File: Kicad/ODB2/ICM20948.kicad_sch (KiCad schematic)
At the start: 2 parts, among them U6 ICM-20948

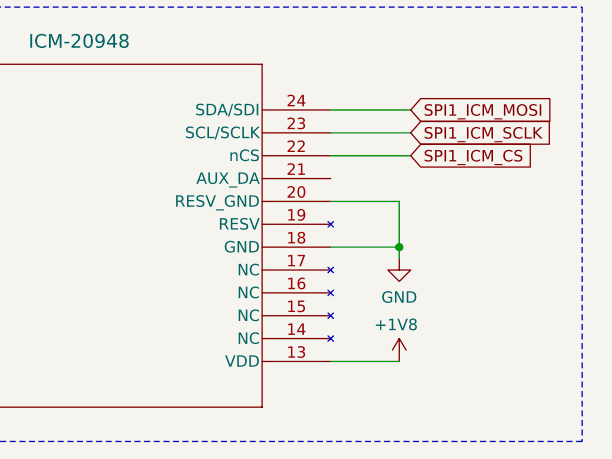
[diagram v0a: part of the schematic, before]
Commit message: add C decoupling
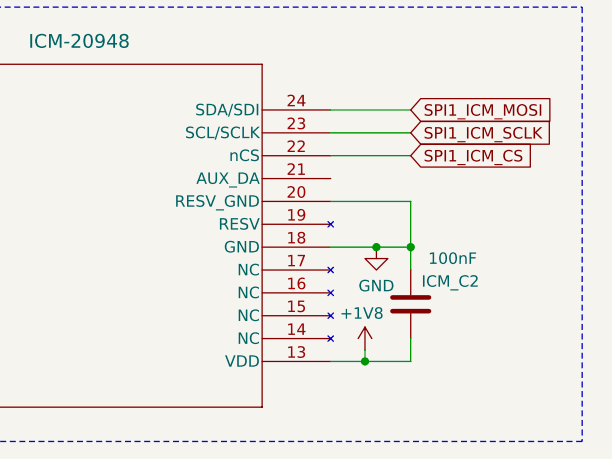
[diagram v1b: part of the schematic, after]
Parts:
- added ICM_C2: 100nF, symbol Device:C
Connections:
- net +1V8: now also ICM_C2.1
- net GND: now also ICM_C2.2
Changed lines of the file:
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@@
+	)
+	(junction
+		(at 110.49 54.61)
+		(diameter 0)
+		(color 0 0 0 0)
 	)
 	(junction
@@
 	)
 	(junction
-		(at 109.22 54.61)
+		(at 105.41 67.31)
 		(diameter 0)
 		(color 0 0 0 0)
 	)
+	(junction
+		(at 106.68 54.61)
+		(diameter 0)
+		(color 0 0 0 0)
+	)
 	(wire
 		(pts
@@
 	(wire
 		(pts
-			(xy 101.6 49.53) (xy 109.22 49.53)
-		)
-		(stroke
-			(width 0)
-			(type default)
-		)
-	)
-	(wire
-		(pts
-			(xy 109.22 55.88) (xy 109.22 54.61)
-		)
-		(stroke
-			(width 0)
-			(type default)
-		)
-	)
-	(wire
-		(pts
-			(xy 101.6 54.61) (xy 109.22 54.61)
+			(xy 106.68 54.61) (xy 110.49 54.61)
+		)
+		(stroke
+			(width 0)
+			(type default)
+		)
+	)
+	(wire
+		(pts
+			(xy 101.6 49.53) (xy 110.49 49.53)
+		)
+		(stroke
+			(width 0)
+			(type default)
+		)
+	)
+	(wire
+		(pts
+			(xy 101.6 54.61) (xy 106.68 54.61)
 		)
 		(stroke
@@
 	(wire
 		(pts
+			(xy 110.49 54.61) (xy 110.49 57.15)
+		)
+		(stroke
+			(width 0)
+			(type default)
+		)
+	)
+	(wire
+		(pts
 			(xy 45.72 64.77) (xy 19.05 64.77)
 		)
@@
 	(wire
 		(pts
-			(xy 109.22 49.53) (xy 109.22 54.61)
+			(xy 105.41 66.04) (xy 105.41 67.31)
+		)
+		(stroke
+			(width 0)
+			(type default)
+		)
+	)
+	(wire
+		(pts
+			(xy 110.49 49.53) (xy 110.49 54.61)
 		)
 		(stroke
@@
 	(wire
 		(pts
-			(xy 101.6 67.31) (xy 109.22 67.31)
-		)
-		(stroke
-			(width 0)
-			(type default)
-		)
-	)
-	(wire
-		(pts
 			(xy 101.6 39.37) (xy 110.49 39.37)
 		)
@@
 	(wire
 		(pts
+			(xy 105.41 67.31) (xy 110.49 67.31)
+		)
+		(stroke
+			(width 0)
+			(type default)
+		)
+	)
+	(wire
+		(pts
 			(xy 101.6 41.91) (xy 110.49 41.91)
+		)
+		(stroke
+			(width 0)
+			(type default)
+		)
+	)
+	(wire
+		(pts
+			(xy 101.6 67.31) (xy 105.41 67.31)
+		)
+		(stroke
+			(width 0)
+			(type default)
+		)
+	)
+	(wire
+		(pts
+			(xy 110.49 67.31) (xy 110.49 64.77)
 		)
 		(stroke
@@
 	(symbol
 		(lib_id "power:+3V3")
-		(at 109.22 67.31 0)
+		(at 105.41 66.04 0)
 		(unit 1)
 		(exclude_from_sim no)
@@
 		(dnp no)
 		(property "Reference" "#PWR056"
-			(at 109.22 71.12 0)
+			(at 105.41 69.85 0)
 			(effects
 				(font
@@
 		)
 		(property "Value" "+1V8"
-			(at 106.426 63.246 0)
+			(at 102.616 61.976 0)
 			(effects
 				(font
@@
 		)
 		(property "Footprint" ""
-			(at 109.22 67.31 0)
+			(at 105.41 66.04 0)
 			(effects
 				(font
@@
 		)
 		(property "Datasheet" ""
-			(at 109.22 67.31 0)
+			(at 105.41 66.04 0)
 			(effects
 				(font
@@
 		)
 		(property "Description" "Power symbol creates a global label with name \"+3V3\""
-			(at 109.22 67.31 0)
+			(at 105.41 66.04 0)
 			(effects
 				(font
@@
 	)
 	(symbol
+		(lib_id "Device:C")
+		(at 110.49 60.96 180)
+		(unit 1)
+		(exclude_from_sim no)
+		(in_bom yes)
+		(on_board yes)
+		(dnp no)
+		(property "Reference" "ICM_C2"
+			(at 118.11 58.42 0)
+			(effects
+				(font
+					(size 1.27 1.27)
+				)
+				(justify left)
+			)
+		)
+		(property "Value" "100nF"
+			(at 117.856 55.88 0)
+			(effects
+				(font
+					(size 1.27 1.27)
+				)
+				(justify left)
+			)
+		)
+		(property "Footprint" ""
+			(at 109.5248 57.15 0)
+			(effects
+				(font
+					(size 1.27 1.27)
+				)
+				(hide yes)
+			)
+		)
+		(property "Datasheet" "~"
+			(at 110.49 60.96 0)
+			(effects
+				(font
+					(size 1.27 1.27)
+				)
+				(hide yes)
+			)
+		)
+		(property "Description" "Unpolarized capacitor"
+			(at 110.49 60.96 0)
+			(effects
+				(font
+					(size 1.27 1.27)
+				)
+				(hide yes)
+			)
+		)
+		(pin "1"
+		)
+		(pin "2"
+		)
+		(instances
+			(project "ODB2"
+				(path "/4b06c5d1-aa8b-48ed-8972-b43a60cfab78/eac5f07f-d6a3-4c95-b286-7cebf46e30db/59725e48-5ae0-4c5e-8605-8169105f55a0"
+					(reference "ICM_C2")
+					(unit 1)
+				)
+			)
+		)
+	)
+	(symbol
 		(lib_id "power:+1V8")
 		(at 40.64 57.15 0)
@@
 	(symbol
 		(lib_id "power:GND")
-		(at 109.22 55.88 0)
+		(at 106.68 54.61 0)
 		(unit 1)
 		(exclude_from_sim no)
@@
 		(dnp no)
 		(property "Reference" "#PWR055"
-			(at 109.22 62.23 0)
+			(at 106.68 60.96 0)
 			(effects
 				(font
@@
 		)
 		(property "Value" "GND"
-			(at 109.22 60.198 0)
+			(at 106.68 58.928 0)
 			(effects
 				(font
@@
 		)
 		(property "Footprint" ""
-			(at 109.22 55.88 0)
+			(at 106.68 54.61 0)
 			(effects
 				(font
@@
 		)
 		(property "Datasheet" ""
-			(at 109.22 55.88 0)
+			(at 106.68 54.61 0)
 			(effects
 				(font
@@
 		)
 		(property "Description" "Power symbol creates a global label with name \"GND\" , ground"
-			(at 109.22 55.88 0)
-			(effects
-				(font
+			(at 106.68 54.61 0)
+			(effects
+				(font

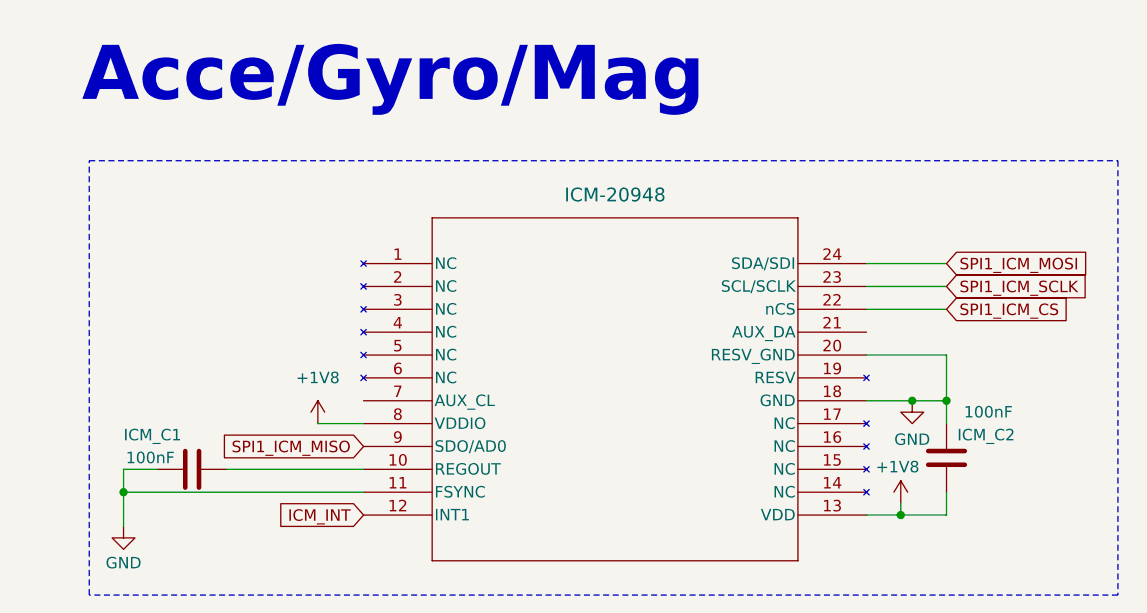
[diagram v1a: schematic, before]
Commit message: merge all sensors to main page + fix NC
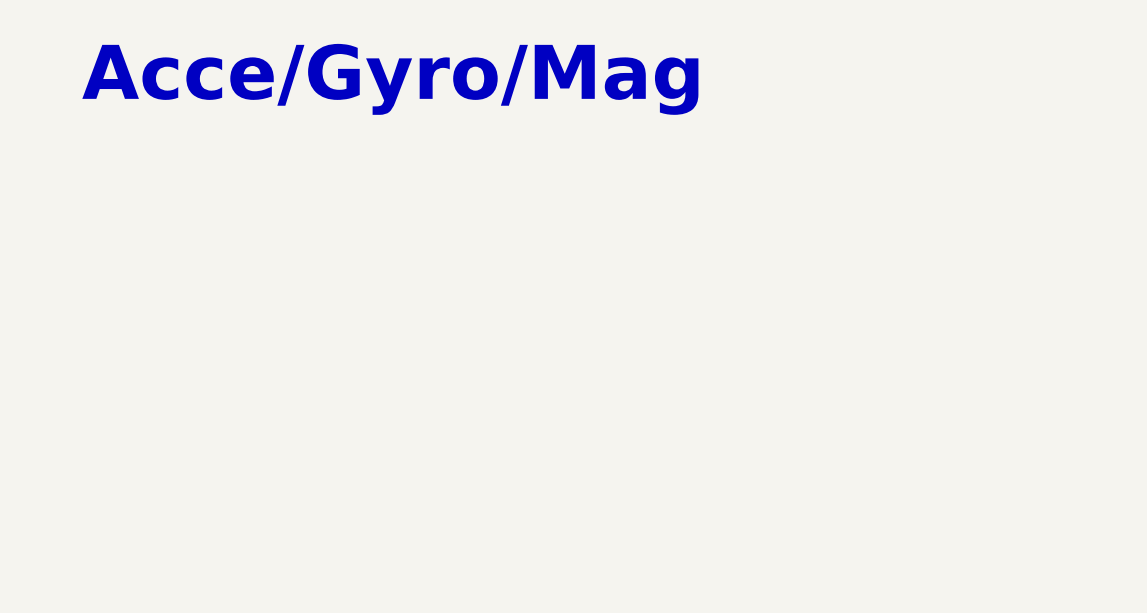
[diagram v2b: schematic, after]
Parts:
- removed ICM_C1, ICM_C2: 100nF, symbol Device:C
- removed U6: ICM-20948, QFN24_3X3X0P9_IVS, symbol ODB_Lib:ICM-20948
